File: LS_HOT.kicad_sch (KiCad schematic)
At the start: 3 parts, among them U4 VNLD5160TR-E

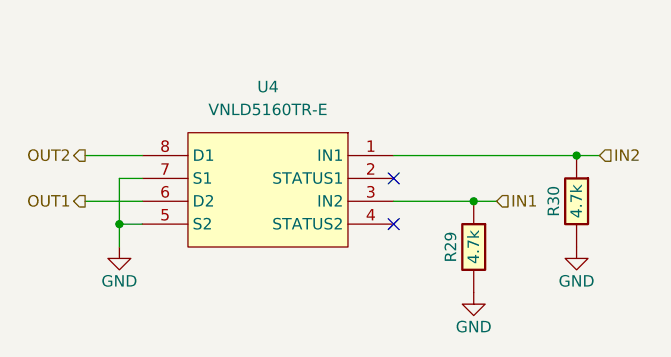
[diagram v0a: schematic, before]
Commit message: colocacion de los componentes en un 90%
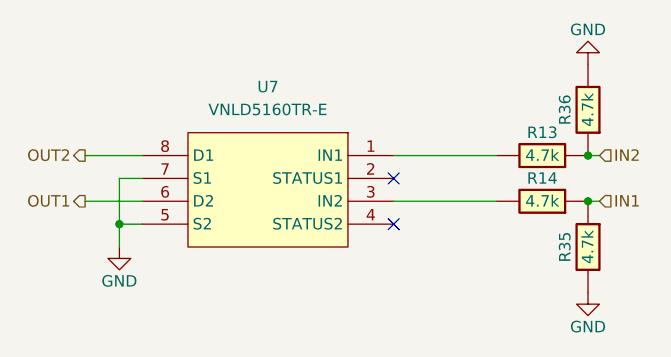
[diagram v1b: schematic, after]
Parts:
- added R13, R14: 4.7k, hellen-one-common:R0603, symbol hellen-one-common:Res
- renumbered R29 to R35, R30 to R36, U4 to U7
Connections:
- net IN1: now also R14.1; no longer U7.3 (IN2)
- net IN2: now also R13.1; no longer U7.1 (IN1)
- new net: R14.2, U7.3 (IN2)
- new net: R13.2, U7.1 (IN1)
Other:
- moved on the sheet: R35, R36
